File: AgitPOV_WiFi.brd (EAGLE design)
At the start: 41.5 x 67.6 mm, 42 parts

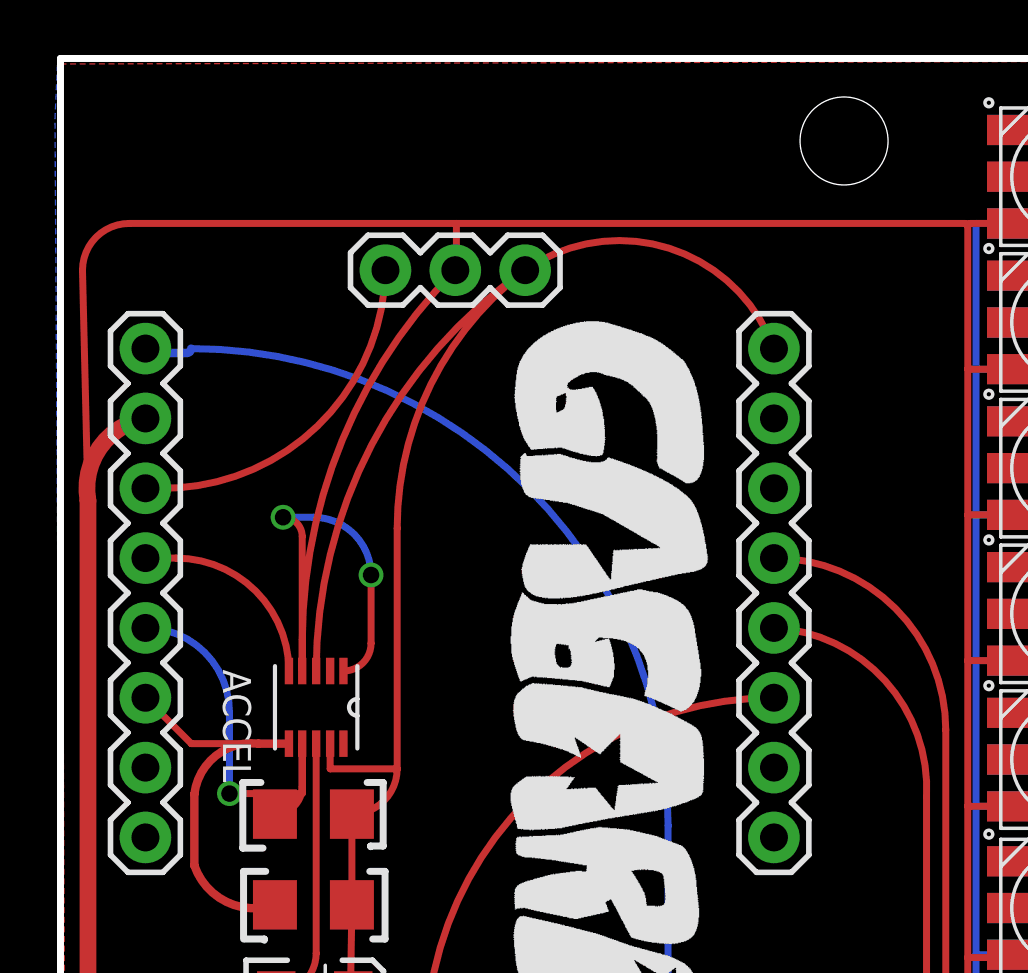
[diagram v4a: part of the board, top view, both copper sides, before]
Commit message: Changed the interrupt pin from D3 to D7
D3 (and D4) when pulled to GND will prevent the Wemos from booting :/.
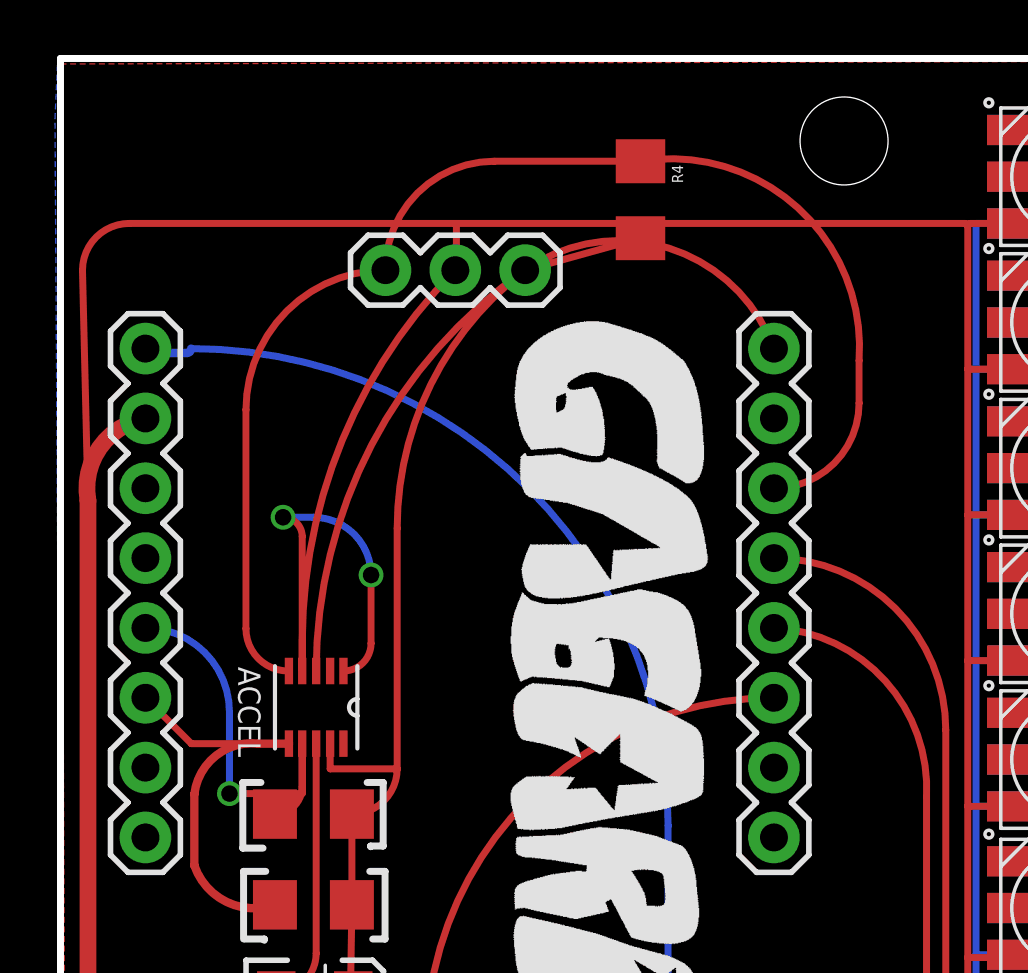
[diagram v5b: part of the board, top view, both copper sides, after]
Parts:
- added R4: 10k, SparkFun-Resistors:1206
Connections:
- net N$5 renamed SCL
- net N$65 renamed SDA
- removed net N$67: ACCEL.5, WEMOS2.4
- new net INT: ACCEL.5, HALL.3, R4.1, WEMOS1.6
- net +3.3V: now also R4.2
- net N$1: now also WEMOS1.7; no longer HALL.3, WEMOS2.3
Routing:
- net INT: track 0.00 -> 44.9 mm
- net N$1: track 11.9 -> 0.00 mm
- net N$67: track 6.92 -> 0.00 mm
- net +3.3V: track 63.9 -> 68.3 mm
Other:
- board text added: "D8"
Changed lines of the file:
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@@
 <setting verticaltext="up"/>
 </settings>
-<grid distance="0.05" unitdist="mm" unit="mm" style="lines" multiple="1" display="yes" altdistance="0.0005" altunitdist="inch" altunit="mm"/>
+<grid distance="1.96850394" unitdist="mil" unit="mil" style="lines" multiple="1" display="yes" altdistance="0.0005" altunitdist="inch" altunit="mm"/>
 <layers>
 <layer number="1" name="Top" color="4" fill="1" visible="yes" active="yes"/>
@@
 <text x="24.05408125" y="46.6369625" size="0.8128" layer="26" rot="MR0">D5</text>
 <text x="23.95408125" y="49.0369625" size="0.8128" layer="26" rot="MR0">D6</text>
-<text x="12.73028125" y="62.0035625" size="0.8128" layer="26" rot="MR0">D4</text>
+<text x="12.73028125" y="62.0035625" size="0.8128" layer="26" rot="MR0">D7</text>
 <text x="19.48888125" y="62.0035625" size="0.8128" layer="26" rot="MR0">+3.3V</text>
 <text x="16.01608125" y="61.9257625" size="0.8128" layer="26" rot="MR0">GND</text>
@@
 <wire x1="12.4206" y1="23.9776" x2="12.3952" y2="23.9776" width="0.254" layer="21"/>
 <wire x1="12.3952" y1="23.9776" x2="12.3952" y2="24.511" width="0.254" layer="21"/>
+<text x="24.02228125" y="54.4139625" size="0.8128" layer="26" rot="MR0">D8</text>
+<text x="24.02228125" y="51.6639625" size="0.8128" layer="26" rot="MR0">D7</text>
 </plain>
 <attributes>
@@
 <attribute name="SUPPLIER" value="FREESCALE SEMICONDUCTOR" x="9.65408125" y="44.2369625" size="1.27" layer="27" rot="R270" display="off"/>
 <attribute name="OC_FARNELL" value="-" x="9.65408125" y="44.2369625" size="1.27" layer="27" rot="R270" display="off"/>
-<attribute name="NAME" x="6.26628125" y="45.6105625" size="1.016" layer="25" ratio="10" rot="SR270"/>
+<attribute name="NAME" x="6.81628125" y="45.7105625" size="0.8128" layer="25" ratio="10" rot="SR270"/>
 </element>
 <element name="R1" library="SparkFun-Resistors" package="1206" value="4.7k" x="9.55408125" y="40.3529625" smashed="yes">
-<attribute name="VALUE" x="5.43008125" y="41.2499625" size="0.8128" layer="27" rot="SR270"/>
+<attribute name="VALUE" x="5.43008125" y="40.6499625" size="0.8128" layer="27" rot="SR270"/>
 </element>
 <element name="R2" library="SparkFun-Resistors" package="1206" value="4.7k" x="9.55408125" y="37.0529625" smashed="yes">
@@
 <attribute name="VALUE" x="5.4214" y="31.7484" size="0.8128" layer="27" rot="SR270"/>
 </element>
+<element name="R4" library="SparkFun-Resistors" package="1206" value="10k" x="21.45" y="62.7" rot="R270"/>
 </elements>
 <signals>
@@
 <wire x1="12.6" y1="41.99888125" x2="10.16208125" y2="41.99888125" width="0.254" layer="1"/>
 <wire x1="10.16208125" y1="41.99888125" x2="10.16208125" y2="42.9161625" width="0.254" layer="1"/>
+<contactref element="R4" pad="2"/>
+<wire x1="17.25408125" y1="60.1369625" x2="21.45" y2="61.3" width="0.254" layer="1"/>
 </signal>
 <signal name="N$6">
@@
 <signal name="N$66">
 </signal>
-<signal name="N$1">
-<contactref element="HALL" pad="3"/>
-<contactref element="WEMOS2" pad="3"/>
-<wire x1="12.17408125" y1="60.1369625" x2="3.94208125" y2="52.2049625" width="0.254" layer="1" curve="-90"/>
-<wire x1="3.94208125" y1="52.2049625" x2="3.44408125" y2="52.2049625" width="0.254" layer="1"/>
-</signal>
-<signal name="N$5">
+<signal name="SCL">
 <contactref element="WEMOS2" pad="6"/>
 <contactref element="ACCEL" pad="6"/>
@@
 <wire x1="5.223" y1="38.48404375" x2="8.15408125" y2="37.0529625" width="0.3048" layer="1" curve="90"/>
 </signal>
-<signal name="N$65">
+<signal name="SDA">
 <contactref element="ACCEL" pad="7"/>
 <contactref element="WEMOS2" pad="5"/>
@@
 <wire x1="6.5" y1="44.06904375" x2="3.44408125" y2="47.1249625" width="0.254" layer="16" curve="90"/>
 </signal>
-<signal name="N$67">
-<contactref element="WEMOS2" pad="4"/>
+<signal name="INT">
 <contactref element="ACCEL" pad="5"/>
-<wire x1="8.66348125" y1="45.5577625" x2="4.55628125" y2="49.6649625" width="0.254" layer="1" curve="90"/>
-<wire x1="4.55628125" y1="49.6649625" x2="3.44408125" y2="49.6649625" width="0.254" layer="1"/>
+<contactref element="HALL" pad="3"/>
+<contactref element="R4" pad="1"/>
+<wire x1="29.4" y1="56.85" x2="21.45" y2="64.1" width="0.254" layer="1" curve="103.37383"/>
+<wire x1="21.45" y1="64.1" x2="16.13711875" y2="64.1" width="0.254" layer="1"/>
+<wire x1="16.13711875" y1="64.1" x2="12.17408125" y2="60.1369625" width="0.254" layer="1" curve="90"/>
+<wire x1="8.66348125" y1="45.5577625" x2="8.6422375" y2="45.5577625" width="0.254" layer="1"/>
+<wire x1="8.6422375" y1="45.5577625" x2="7.1" y2="47.1" width="0.254" layer="1" curve="-90"/>
+<wire x1="7.1" y1="47.1" x2="7.1" y2="55.06288125" width="0.254" layer="1"/>
+<wire x1="7.1" y1="55.06288125" x2="12.17408125" y2="60.1369625" width="0.254" layer="1" curve="-90"/>
+<contactref element="WEMOS1" pad="6"/>
+<wire x1="29.4" y1="56.85" x2="29.4" y2="55.30088125" width="0.254" layer="1"/>
+<wire x1="29.4" y1="55.30088125" x2="26.30408125" y2="52.2049625" width="0.254" layer="1" curve="-90"/>
 </signal>
 <signal name="PULLDOWN">
@@
 <wire x1="6.39828125" y1="11.8369625" x2="2.40488125" y2="7.8435625" width="0.6096" layer="16" curve="90"/>
 </signal>
+<signal name="N$1">
+<contactref element="WEMOS1" pad="7"/>
+</signal>
 </signals>
